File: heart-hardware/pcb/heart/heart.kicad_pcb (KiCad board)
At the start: 4 copper layers, 49.5 x 44 mm, 66 parts, among them J1 3V0, J2 DIO, J3 CLK, J4 GND, J5 TOUCH_KEY, SW1 SW_SPDT, U1 STM32L031F6Px, U2 TCA6416APWR, U3 LIS3DH, U4 Holtek-Semicon-BS812A-1

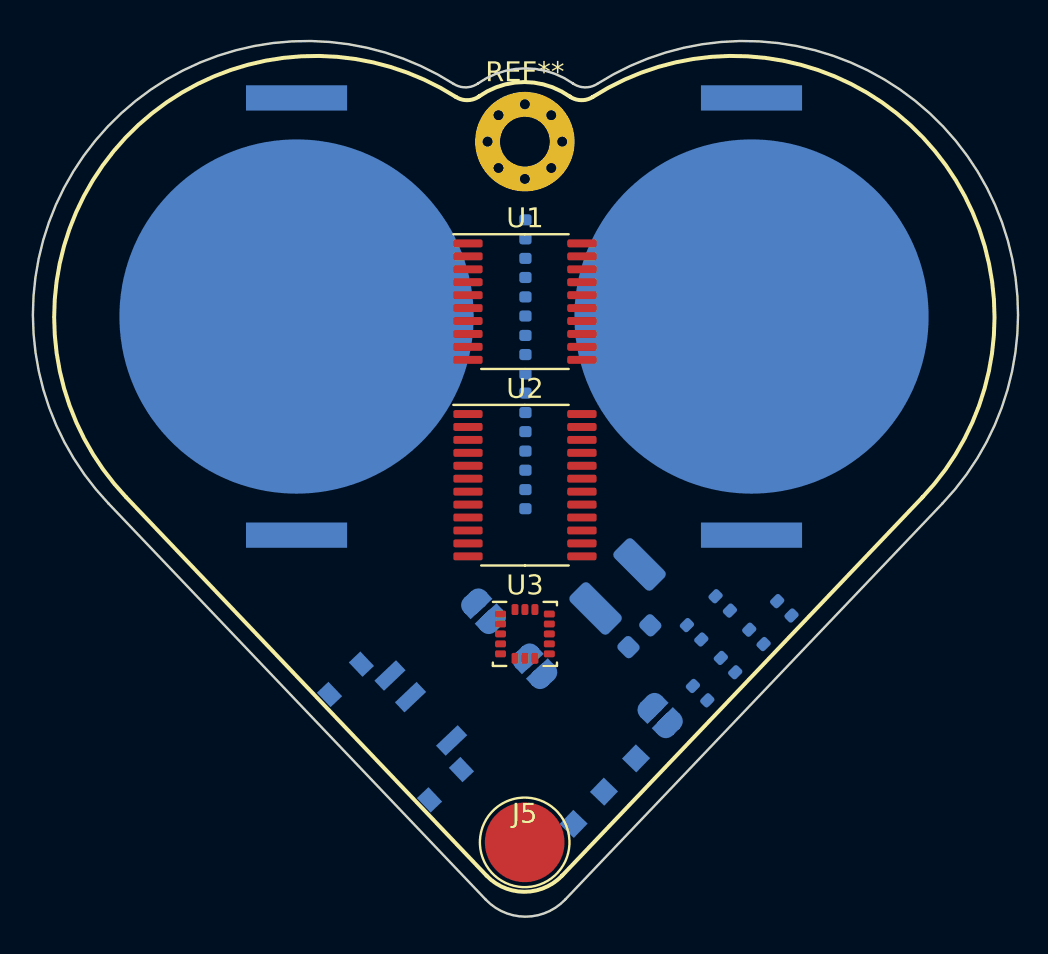
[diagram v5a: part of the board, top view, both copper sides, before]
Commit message: Changed battery from 2x CR2032 to 1x CR2450
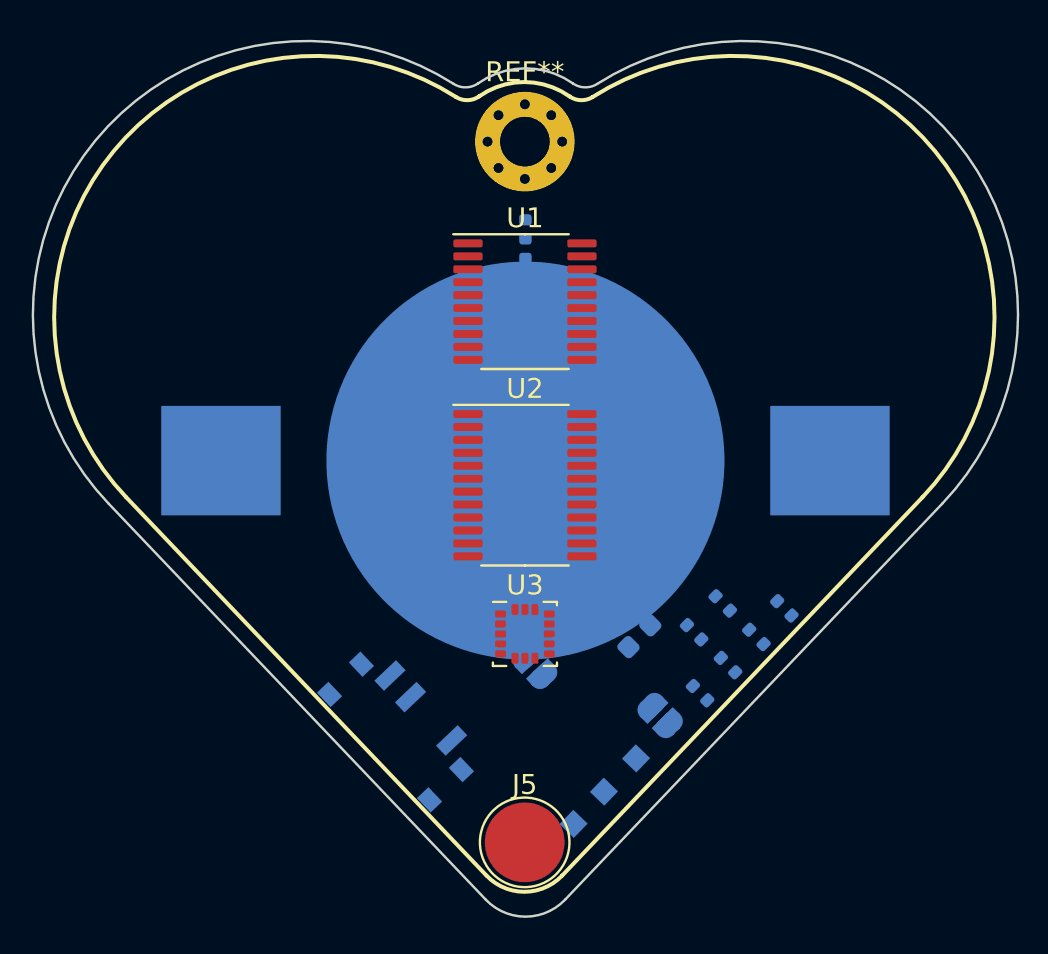
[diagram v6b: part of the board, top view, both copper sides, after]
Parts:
- removed BT2: CR2032, Battery:BatteryHolder_Keystone_3034_1x20mm
- BT1: value CR2032 -> CR2450; footprint Battery:BatteryHolder_Keystone_3034_1x20mm -> Battery:BatteryHolder_Keystone_3008_1x2450
- moved BT1 13.5 mm to (157.4, 134.2), turned to 0 degrees

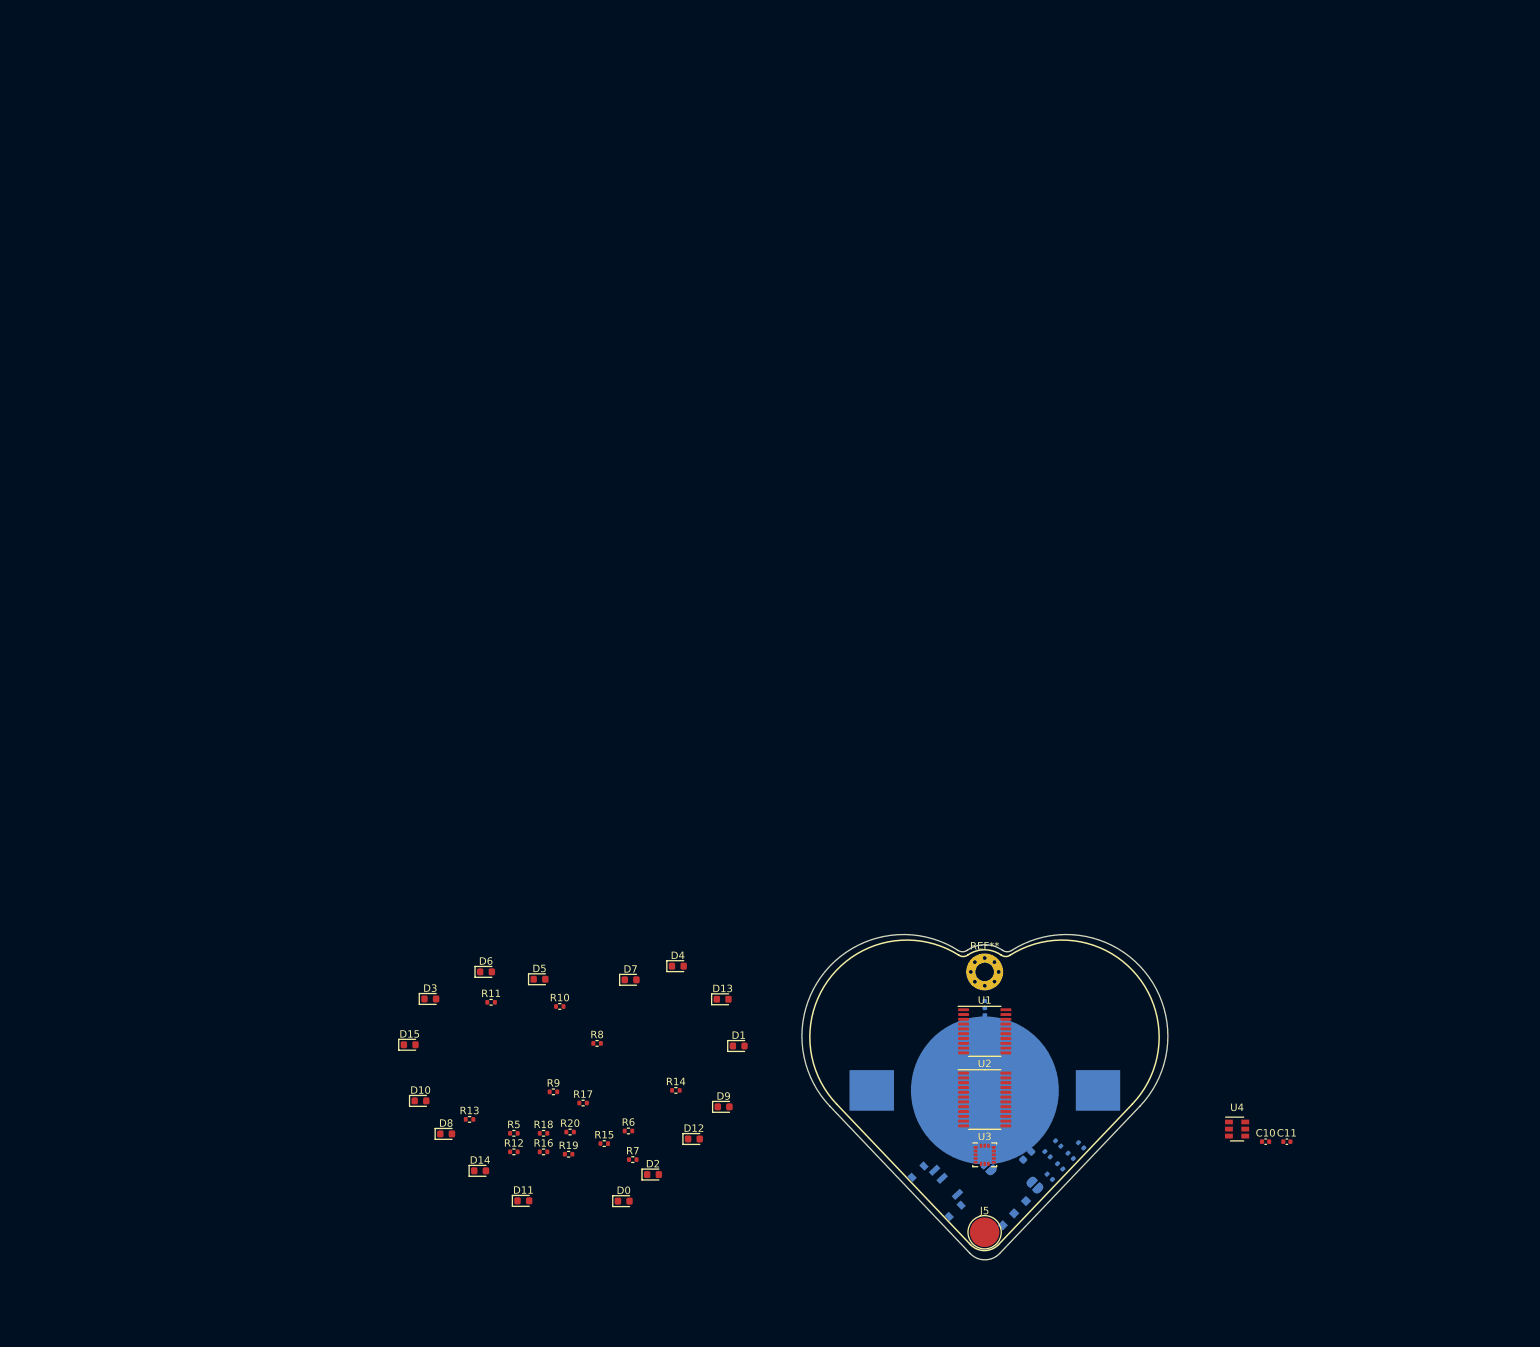
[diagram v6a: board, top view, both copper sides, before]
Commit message: New heart shape, battery change, top layer component placed v1
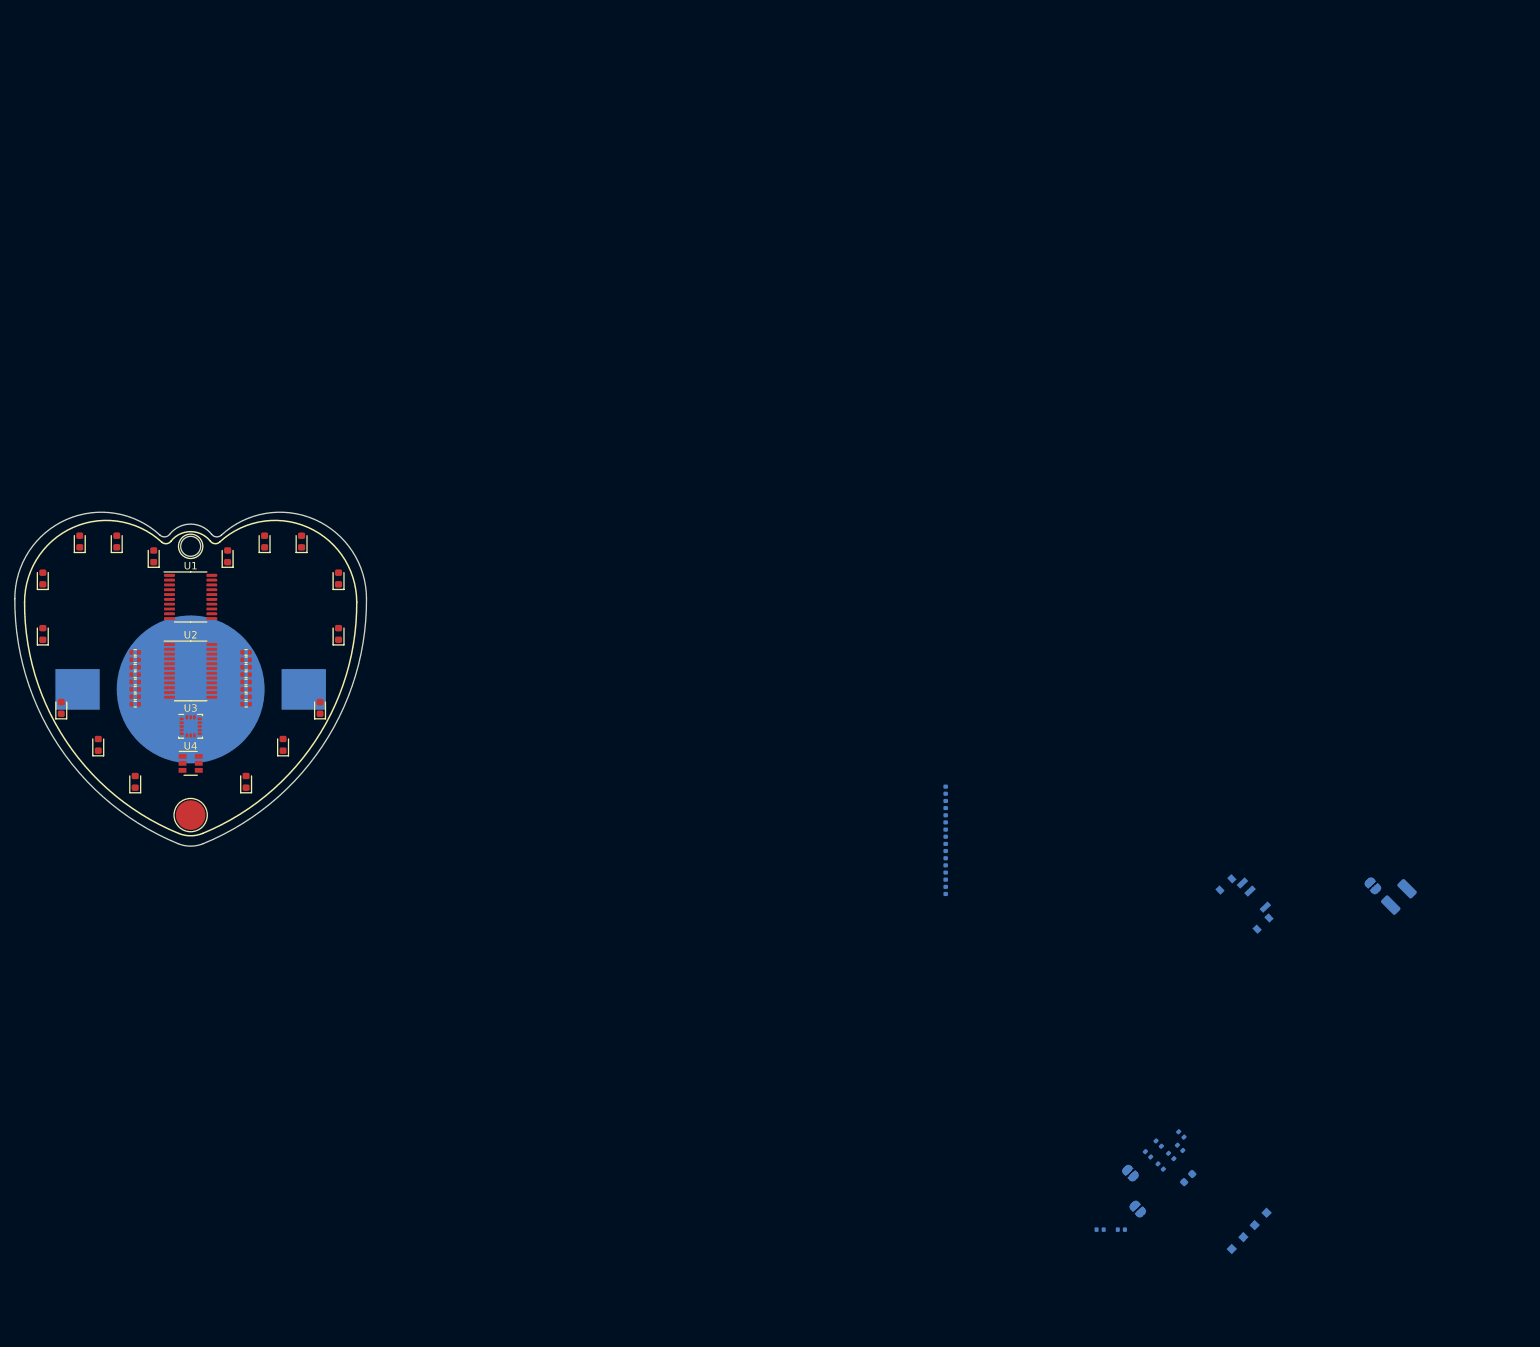
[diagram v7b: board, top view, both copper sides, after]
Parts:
- removed the R13 at (87.7, 138.2)
- removed the REF** at (157.4, 118.2)
- added R8: R, Resistor_SMD:R_0402_1005Metric, F.Cu at (57.5, 82.0)
- added REF**: MountingHole_2.7mm, MountingHole:MountingHole_2.7mm, F.Cu at (50.0, 60.6)
- C10, C11: moved to B.Cu
- moved U4 149.9 mm to (50.0, 90.0)
- moved U1 122.4 mm to (50.0, 67.5)
- moved U2 122.0 mm to (50.0, 77.5)
- moved U3 122.0 mm to (50.0, 85.0)
- moved J5 121.3 mm to (50.0, 97.0)
- moved BT1 120.3 mm to (50.0, 80.0), turned to 180 degrees
- moved D2 115.5 mm to (35.0, 60.0), turned to 90 degrees
- moved D1 108.3 mm to (40.0, 60.0), turned to 90 degrees
- moved D0 107.9 mm to (45.0, 62.0), turned to 90 degrees
- moved D4 96.9 mm to (30.0, 72.5), turned to 90 degrees
- moved R1 95.4 mm to (42.5, 76.0), turned to 180 degrees
- moved R3 90.9 mm to (42.5, 78.0), turned to 180 degrees
- moved D14 90.0 mm to (60.0, 60.0), turned to 90 degrees
- moved D12 89.8 mm to (70.0, 65.0), turned to 90 degrees
- moved D13 84.1 mm to (65.0, 60.0), turned to 90 degrees
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- renumbered R7 to R1, R15 to R10, R16 to R11, R17 to R12, R18 to R13, R19 to R14, R20 to R15, R5 to R2, R1 to R21, R2 to R22, R3 to R23, R4 to R24, R21 to R25, R22 to R26, R6 to R3, R9 to R4, R8 to R4, R10 to R5, R11 to R6, R12 to R7, R14 to R9
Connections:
- D0 pad 2: Net-(D0-Pad2) -> +3V0
- D1 pad 2: Net-(D1-Pad2) -> +3V0
- D10 pad 2: Net-(D10-Pad2) -> +3V0
- D11 pad 2: Net-(D11-Pad2) -> +3V0
- D12 pad 2: Net-(D12-Pad2) -> +3V0
- D13 pad 2: Net-(D13-Pad2) -> +3V0
- D14 pad 2: Net-(D14-Pad2) -> +3V0
- D15 pad 2: Net-(D15-Pad2) -> +3V0
- D2 pad 2: Net-(D2-Pad2) -> +3V0
- D3 pad 2: Net-(D3-Pad2) -> +3V0
- D4 pad 2: Net-(D4-Pad2) -> +3V0
- D5 pad 2: Net-(D5-Pad2) -> +3V0
- D6 pad 2: Net-(D6-Pad2) -> +3V0
- D7 pad 2: Net-(D7-Pad2) -> +3V0
- D8 pad 2: Net-(D8-Pad2) -> +3V0
- D9 pad 2: Net-(D9-Pad2) -> +3V0
- R1 pad 1: Net-(D1-Pad2) -> Net-(R1-Pad1)
- R1 pad 2: +3V0 -> Net-(D1-Pad1)
- R10 pad 1: Net-(D10-Pad2) -> Net-(R10-Pad1)
- R10 pad 2: +3V0 -> Net-(D10-Pad1)
- R11 pad 1: Net-(D11-Pad2) -> Net-(R11-Pad1)
- R11 pad 2: +3V0 -> Net-(D11-Pad1)
- R12 pad 1: Net-(D12-Pad2) -> Net-(R12-Pad1)
- R12 pad 2: +3V0 -> Net-(D12-Pad1)
- R13 pad 1: Net-(D13-Pad2) -> Net-(R13-Pad1)
- R13 pad 2: +3V0 -> Net-(D13-Pad1)
- R14 pad 1: Net-(D14-Pad2) -> Net-(R14-Pad1)
- R14 pad 2: +3V0 -> Net-(D14-Pad1)
- R15 pad 1: Net-(D15-Pad2) -> Net-(R15-Pad1)
- R15 pad 2: +3V0 -> Net-(D15-Pad1)
- R2 pad 1: Net-(D2-Pad2) -> Net-(R2-Pad1)
- R2 pad 2: +3V0 -> Net-(D2-Pad1)
- R3 pad 1: Net-(D3-Pad2) -> Net-(R3-Pad1)
- R3 pad 2: +3V0 -> Net-(D3-Pad1)
- R4 pad 1: Net-(D4-Pad2) -> Net-(R4-Pad1)
- R4 pad 2: +3V0 -> Net-(D4-Pad1)
- R4 pad 1: Net-(D0-Pad2) -> Net-(R0-Pad1)
- R4 pad 2: +3V0 -> Net-(D0-Pad1)
- R5 pad 1: Net-(D5-Pad2) -> Net-(R5-Pad1)
- R5 pad 2: +3V0 -> Net-(D5-Pad1)
- R6 pad 1: Net-(D6-Pad2) -> Net-(R6-Pad1)
- R6 pad 2: +3V0 -> Net-(D6-Pad1)
- R7 pad 1: Net-(D7-Pad2) -> Net-(R7-Pad1)
- R7 pad 2: +3V0 -> Net-(D7-Pad1)
- R9 pad 1: Net-(D9-Pad2) -> Net-(R9-Pad1)
- R9 pad 2: +3V0 -> Net-(D9-Pad1)
- U2 pad 10: Net-(D6-Pad1) -> Net-(R6-Pad1)
- U2 pad 11: Net-(D7-Pad1) -> Net-(R7-Pad1)
- U2 pad 13: Net-(D8-Pad1) -> Net-(R8-Pad1)
- U2 pad 14: Net-(D9-Pad1) -> Net-(R9-Pad1)
- U2 pad 15: Net-(D10-Pad1) -> Net-(R10-Pad1)
- U2 pad 16: Net-(D11-Pad1) -> Net-(R11-Pad1)
- U2 pad 17: Net-(D12-Pad1) -> Net-(R12-Pad1)
- U2 pad 18: Net-(D13-Pad1) -> Net-(R13-Pad1)
- U2 pad 19: Net-(D14-Pad1) -> Net-(R14-Pad1)
- U2 pad 20: Net-(D15-Pad1) -> Net-(R15-Pad1)
- U2 pad 4: Net-(D0-Pad1) -> Net-(R0-Pad1)
- U2 pad 5: Net-(D1-Pad1) -> Net-(R1-Pad1)
- U2 pad 6: Net-(D2-Pad1) -> Net-(R2-Pad1)
- U2 pad 7: Net-(D3-Pad1) -> Net-(R3-Pad1)
- U2 pad 8: Net-(D4-Pad1) -> Net-(R4-Pad1)
- U2 pad 9: Net-(D5-Pad1) -> Net-(R5-Pad1)
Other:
- board size 49.5 x 44 mm -> 47.6 x 45.2 mm
- board text removed: "OFF"
- board text removed: "ON"

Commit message: All components initially placed
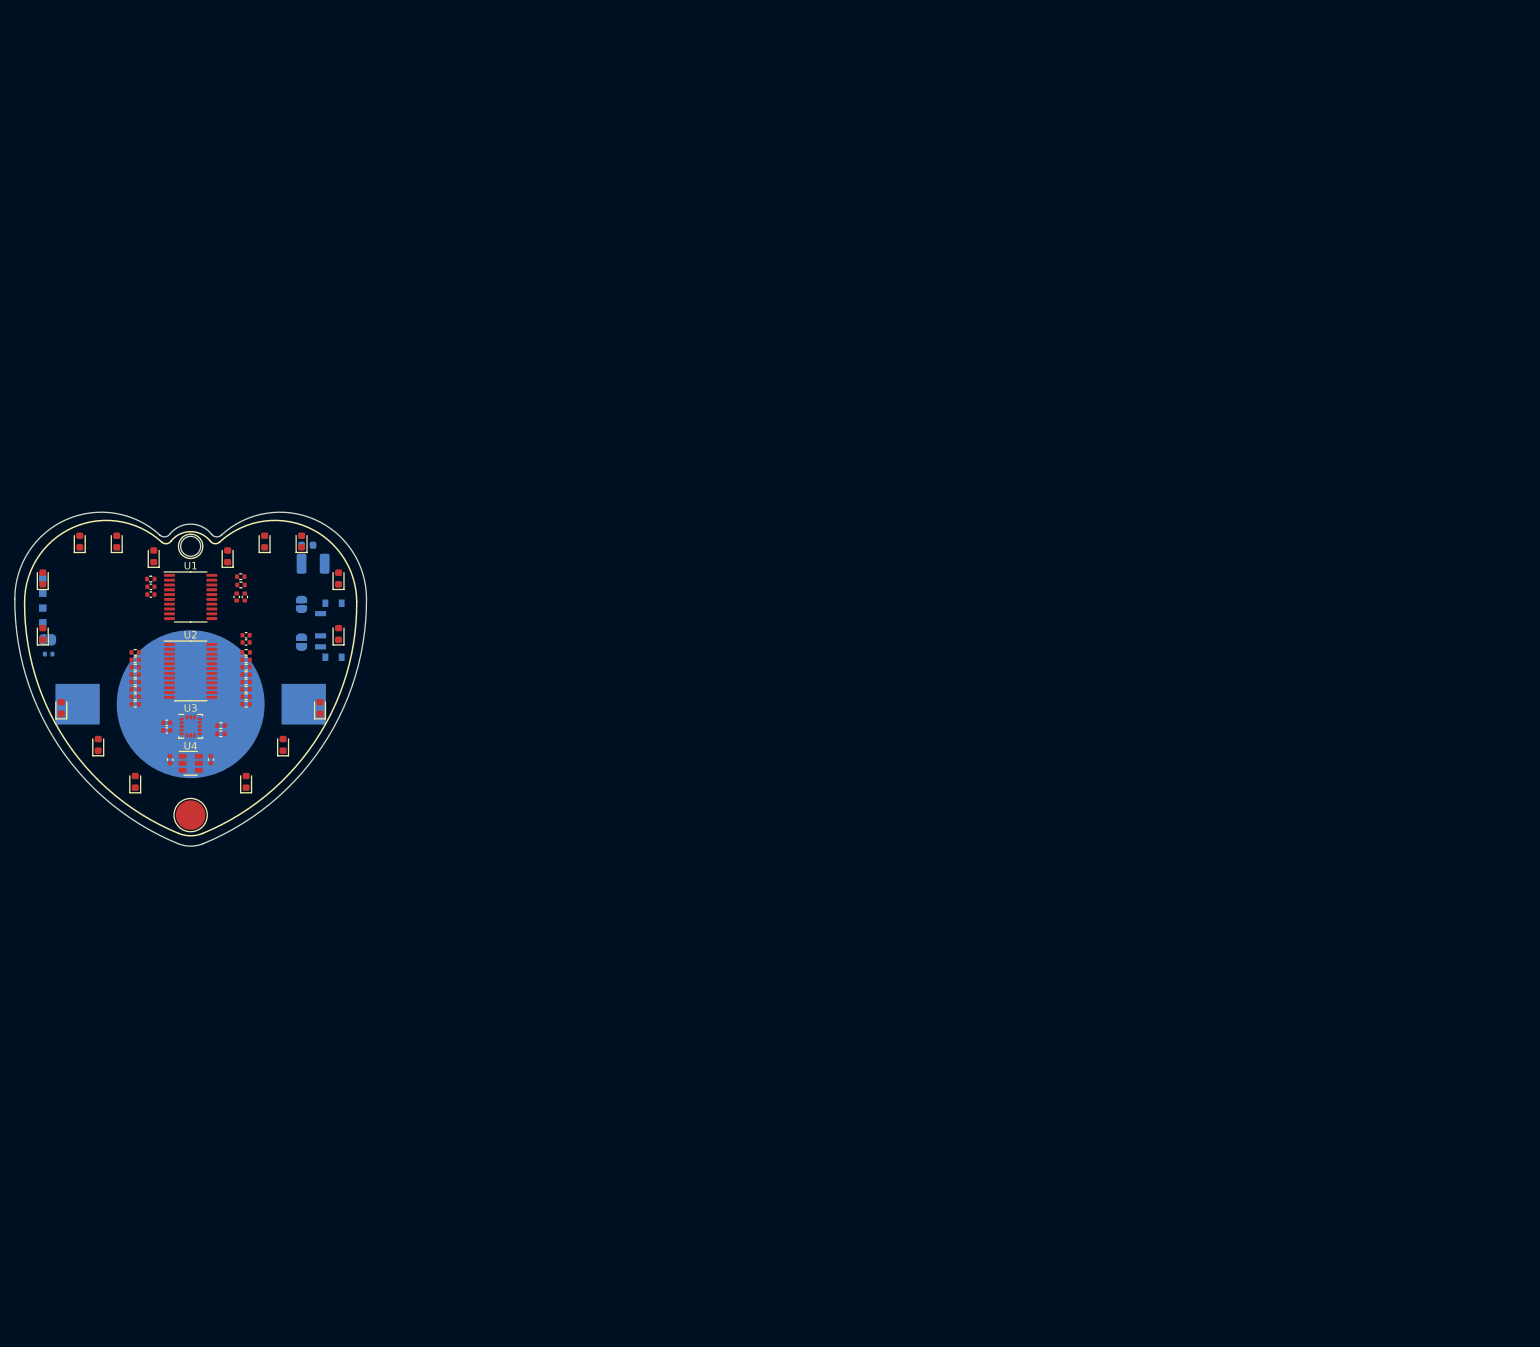
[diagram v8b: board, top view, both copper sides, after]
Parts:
- added REF**: KiCad-Logo2_5mm_SilkScreen, Symbol:KiCad-Logo2_5mm_SilkScreen, B.Cu at (50.0, 66.0)
- C10, C11, C2, C3, C4, C5, C6, C7, C8, C9, R21, R22, R23, R25, R26: moved to F.Cu
- CR2450: renamed from BT1; value CR2450 -> BT1
- moved J1 184.6 mm to (30.0, 65.0), turned to 270 degrees
- moved J3 184.3 mm to (30.0, 67.0), turned to 270 degrees
- moved J2 183.9 mm to (30.0, 69.0), turned to 270 degrees
- moved Je 183.8 mm to (30.0, 71.0), turned to 270 degrees
- moved R24 167.0 mm to (30.8, 75.2), turned to 180 degrees
- moved JP3 163.3 mm to (30.6, 73.3), turned to 0 degrees
- moved R21 158.0 mm to (44.6, 65.1), turned to 0 degrees
- moved C0 153.6 mm to (66.6, 63.0), turned to 0 degrees
- moved JP1 148.6 mm to (65.0, 73.6), turned to 90 degrees
- moved R23 148.3 mm to (56.8, 64.8), turned to 180 degrees
- moved R22 147.3 mm to (56.8, 65.9), turned to 0 degrees
- moved C1 146.7 mm to (65.8, 60.5), turned to 0 degrees
- moved C11 143.5 mm to (47.2, 89.5), turned to 90 degrees
- moved JP2 139.6 mm to (65.0, 68.5), turned to 90 degrees
- moved R25 138.4 mm to (54.1, 86.0), turned to 0 degrees
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- renumbered J4 to Je
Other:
- board text added: "E"
- board text added: "K"
